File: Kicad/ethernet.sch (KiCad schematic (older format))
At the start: 1 part

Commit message: Completed Audio sheet.
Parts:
- gave numbers to parts that had none: 1
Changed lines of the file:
@@
 Sheet 3 9
 Title ""
-Date ""
+Date "2020-12-20"
 Rev ""
-Comp ""
-Comment1 ""
-Comment2 ""
+Comp "https://neotron-compute.github.io/"
+Comment1 "Licenced as CC BY-SA"
+Comment2 "Copyright (c) The Neotron Developers, 2020"
 Comment3 ""
 Comment4 ""
 $EndDescr
 $Comp
-L Connector:RJ45_Amphenol_RJMG1BD3B8K1ANR J?
+L Connector:RJ45_Amphenol_RJMG1BD3B8K1ANR J301
 U 1 1 5FDF0883
 P 2650 2400
-F 0 "J?" V 2696 2988 50  0000 L CNN
+F 0 "J301" V 2696 2988 50  0000 L CNN
 F 1 "RJ45_Amphenol_RJMG1BD3B8K1ANR" V 3635 1740 50  0000 L CNN
 F 2 "Connector_RJ:RJ45_Amphenol_RJMG1BD3B8K1ANR" H 2650 3100 50  0001 C CNN

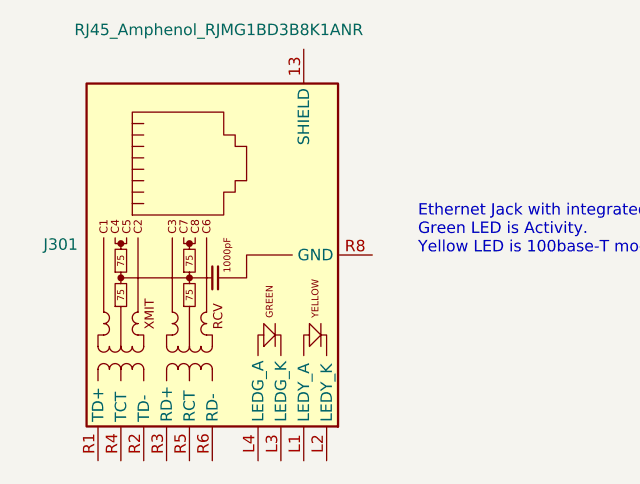
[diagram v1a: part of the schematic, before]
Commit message: Brought in RS232 circuit from Neotron 32.
Also updated 3D models.
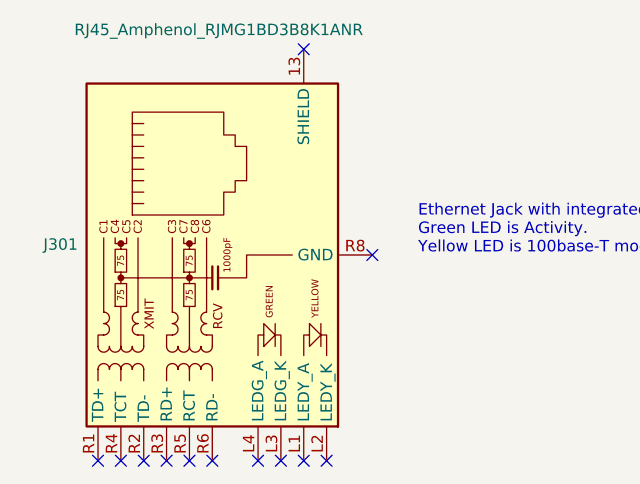
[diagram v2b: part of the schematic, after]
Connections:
- no-connect marks 0 -> 12
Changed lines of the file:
@@
 Text Notes 3550 2400 0    50   ~ 0
 Ethernet Jack with integrated magnetics.\nGreen LED is Activity.\nYellow LED is 100base-T mode active.
+NoConn ~ 2150 3300
+NoConn ~ 2250 3300
+NoConn ~ 2350 3300
+NoConn ~ 2450 3300
+NoConn ~ 2550 3300
+NoConn ~ 2650 3300
+NoConn ~ 2850 3300
+NoConn ~ 2950 3300
+NoConn ~ 3050 3300
+NoConn ~ 3150 3300
+NoConn ~ 3350 2400
+NoConn ~ 3050 1500
 $EndSCHEMATC

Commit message: Updating BOM with parts.
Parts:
- J301: DNP (none) -> 0
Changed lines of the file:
@@
 F 2 "Connector_RJ:RJ45_Amphenol_RJMG1BD3B8K1ANR" H 2650 3100 50  0001 C CNN
 F 3 "https://www.amphenolcanada.com/ProductSearch/Drawings/AC/RJMG1BD3B8K1ANR.PDF" H 2650 3200 50  0001 C CNN
+F 4 "0" H 2650 2400 50  0001 C CNN "DNP"
 	1    2650 2400
 	0    -1   -1   0

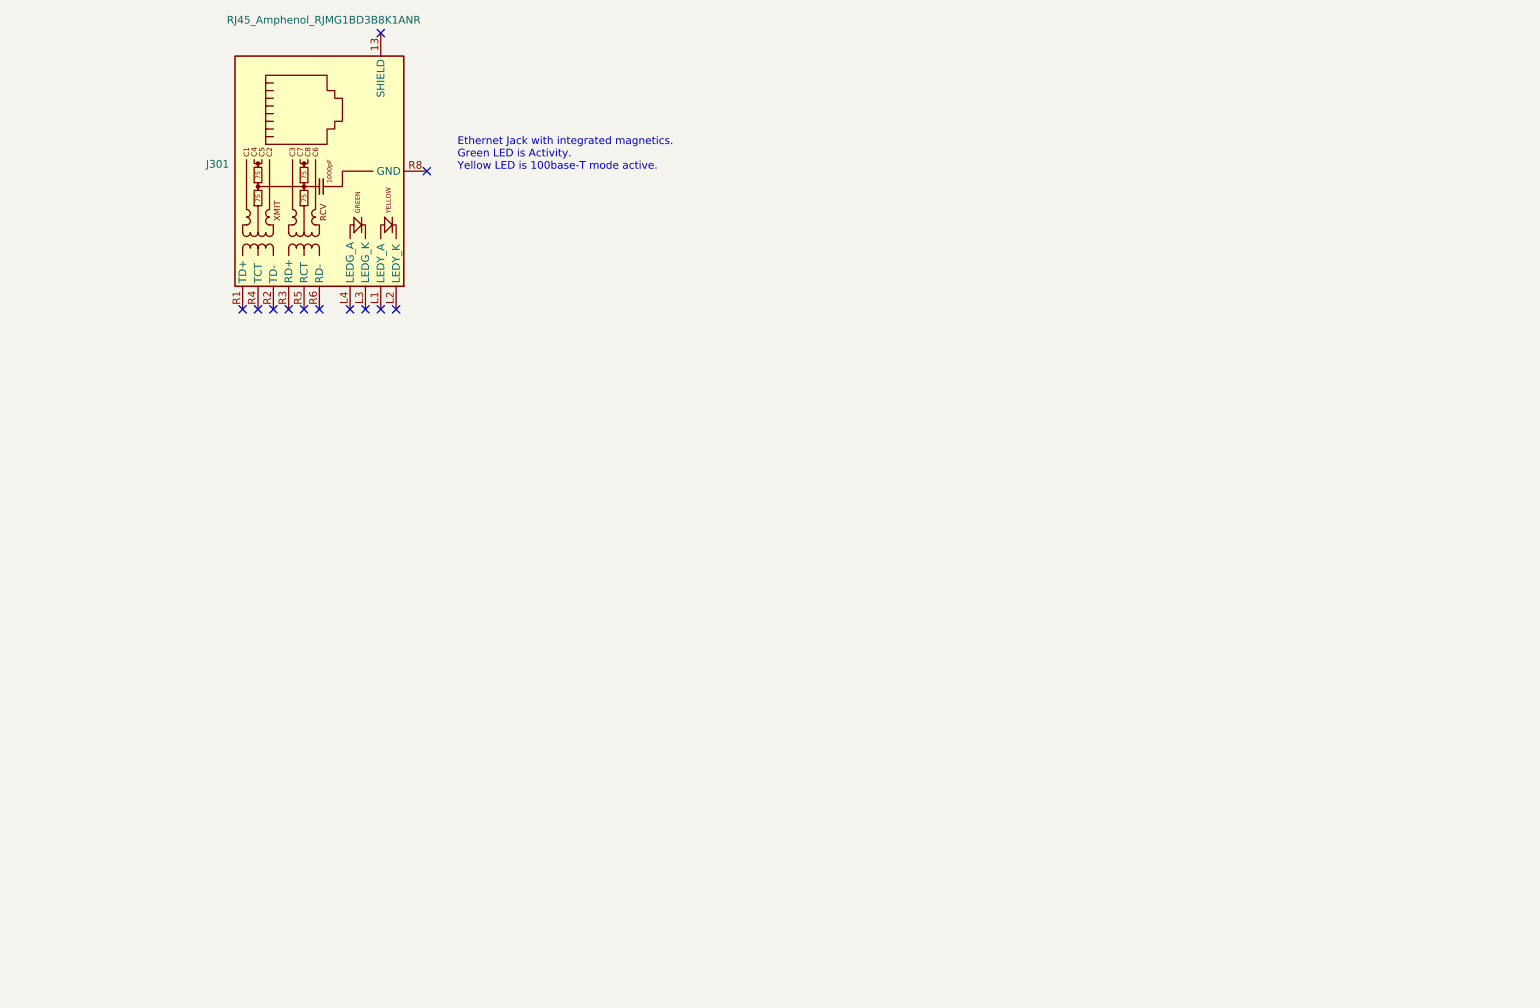
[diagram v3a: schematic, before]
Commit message: Wired up Ethernet sheet.
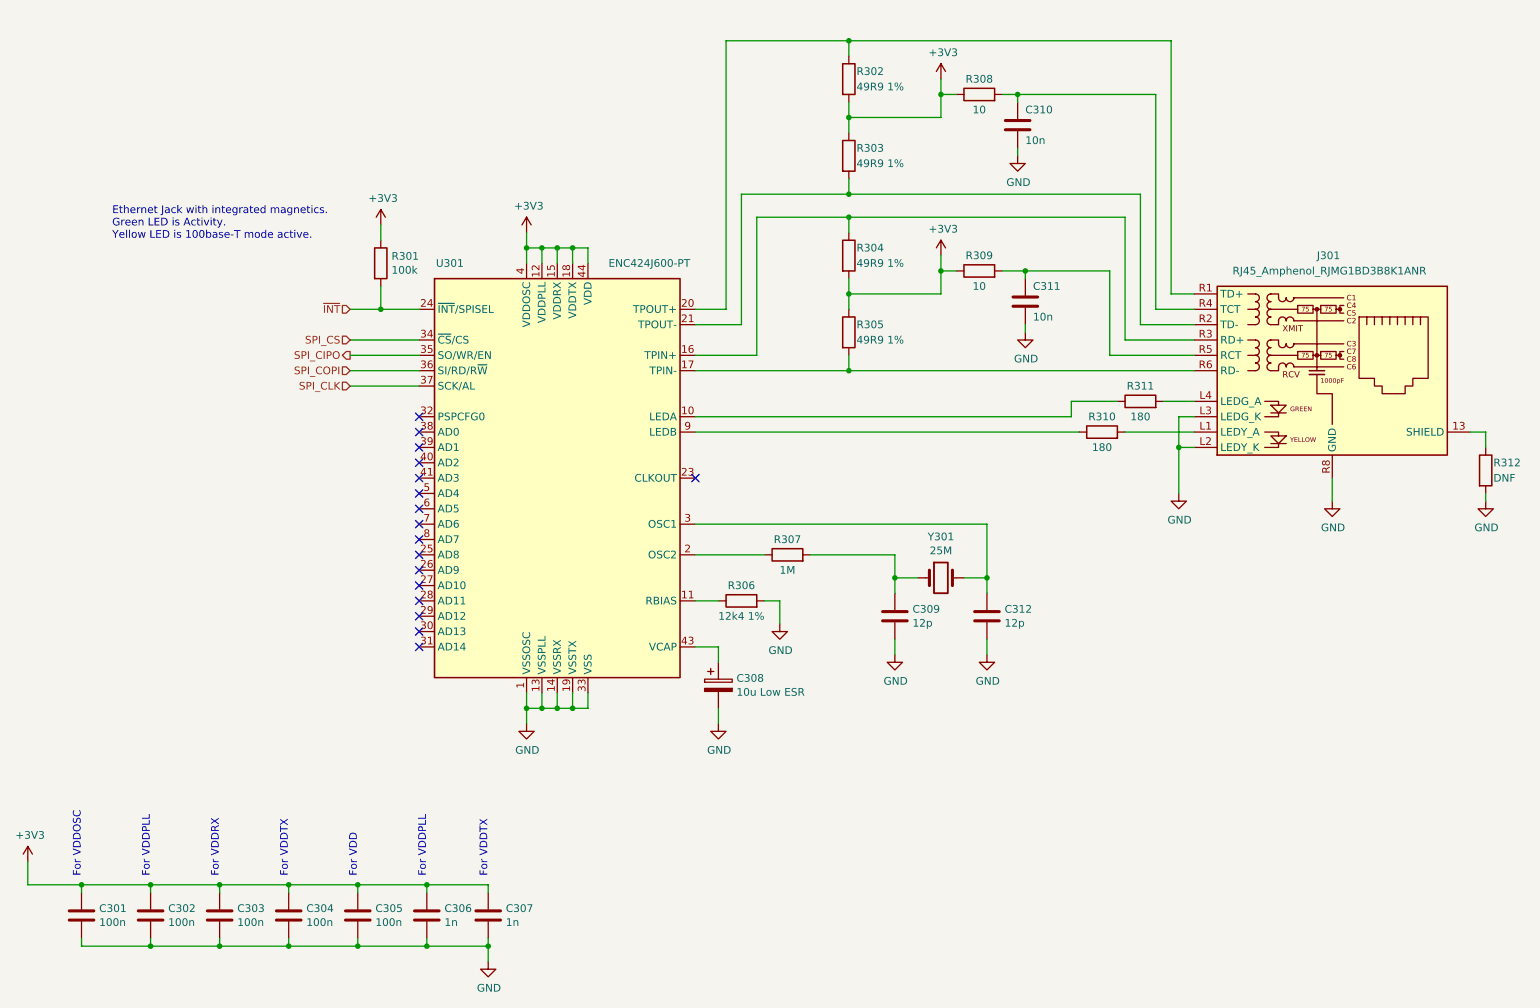
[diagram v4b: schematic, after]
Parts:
- added C301, C302, C303, C304, C305: 100n, Capacitor_SMD:C_0805_2012Metric_Pad1.15x1.40mm_HandSolder, symbol Device:C
- added C306, C307: 1n, Capacitor_SMD:C_0805_2012Metric_Pad1.15x1.40mm_HandSolder, symbol Device:C
- added C308: 10u Low ESR, Capacitor_THT:CP_Radial_D6.3mm_P2.50mm, symbol Device:CP
- added C309, C312: 12p, Capacitor_SMD:C_0805_2012Metric_Pad1.15x1.40mm_HandSolder, symbol Device:C
- added C310, C311: 10n, Capacitor_SMD:C_0805_2012Metric_Pad1.15x1.40mm_HandSolder, symbol Device:C
- added R301: 100k, Resistor_SMD:R_0805_2012Metric_Pad1.15x1.40mm_HandSolder, symbol Device:R
- added R302, R303, R304, R305: 49R9 1%, Resistor_SMD:R_0805_2012Metric_Pad1.15x1.40mm_HandSolder, symbol Device:R
- added R306: 12k4 1%, Resistor_SMD:R_0805_2012Metric_Pad1.15x1.40mm_HandSolder, symbol Device:R
- added R307: 1M, Resistor_SMD:R_0805_2012Metric_Pad1.15x1.40mm_HandSolder, symbol Device:R
- added R308, R309: 10, Resistor_SMD:R_0805_2012Metric_Pad1.15x1.40mm_HandSolder, symbol Device:R
- added R310, R311: 180, Resistor_SMD:R_0805_2012Metric_Pad1.15x1.40mm_HandSolder, symbol Device:R
- added R312: DNF, Resistor_SMD:R_0805_2012Metric_Pad1.15x1.40mm_HandSolder, symbol Device:R
- added U301: ENC424J600-PT, Package_QFP:TQFP-44_10x10mm_P0.8mm, symbol Interface_Ethernet:ENC424J600-PT
- added Y301: 25M, Crystal:Crystal_HC49-4H_Vertical, symbol Device:Crystal
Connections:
- net at J301.13 (SHIELD): now also R312.1
- net at J301.L1 (LEDY_A): now also R310.2
- net GND: now reaches J301.L2 (LEDY_K)
- net GND: now also J301.L3 (LEDG_K), J301.R8 (GND), C301.2, C302.2, C303.2, C304.2, C305.2, C306.2, C307.2, C308.2, C309.2, C310.2, C311.2, C312.2, R306.2, R312.2, U301.1 (VSSOSC), U301.13 (VSSPLL), U301.14 (VSSRX), U301.19 (VSSTX), U301.22 (VSSTX), U301.33 (VSS), U301.42 (VSS)
- net at J301.L4 (LEDG_A): now also R311.2
- net at J301.R1 (TD+): now also R302.1, U301.20 (TPOUT+)
- net at J301.R2 (TD-): now also R303.2, U301.21 (TPOUT-)
- net at J301.R3 (RD+): now also R304.1, U301.16 (TPIN+)
- net at J301.R4 (TCT): now also C310.1, R308.2
- net at J301.R5 (RCT): now also C311.1, R309.2
- net at J301.R6 (RD-): now also R305.2, U301.17 (TPIN-)
- new net: R311.1, U301.10 (LEDA)
- new net: R306.1, U301.11 (RBIAS)
- new net: R307.1, U301.2 (OSC2)
- new net: C312.1, U301.3 (OSC1), Y301.2
- new net: C308.1, U301.43 (VCAP)
- new net: R310.1, U301.9 (LEDB)
- new net: C309.1, R307.2, Y301.1
- new net +3V3: C301.1, C302.1, C303.1, C304.1, C305.1, C306.1, C307.1, R301.1, R302.2, R303.1, R304.2, R305.1, R308.1, R309.1, U301.12 (VDDPLL), U301.15 (VDDRX), U301.18 (VDDTX), U301.4 (VDDOSC), U301.44 (VDD)
- new net SPI_CIPO: U301.35 (SO/WR/EN)
- new net SPI_CLK: U301.37 (SCK/AL)
- new net SPI_COPI: U301.36 (SI/RD/R~W)
- new net SPI_CS: U301.34 (~CS~/CS)
- new net ~INT: R301.2, U301.24 (~INT~/SPISEL)
- no-connect marks 12 -> 17
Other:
- note added: "For VDD"
- note added: "For VDDOSC"
- note added: "For VDDPLL"
- note added: "For VDDRX"
- note added: "For VDDTX"
- moved on the sheet: J301
